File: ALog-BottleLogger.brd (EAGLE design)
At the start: 120.7 x 44.5 mm, 106 parts, among them IC2 ATMEGA644M, J6 5.5x2.1mm Barrel, Q10 MOSFET_PCH-IRLML2244, Q11 MOSFET-NCH-BSS138, Q12 MOSFET_PCH-IRLML2244, Q5 MOSFET_PCH-IRLML2244, Q7 MOSFET_PCH-IRLML2244, Q8 MOSFET-NCH-BSS138, Q9 MOSFET-NCH-BSS138, U2 FT231X-Q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

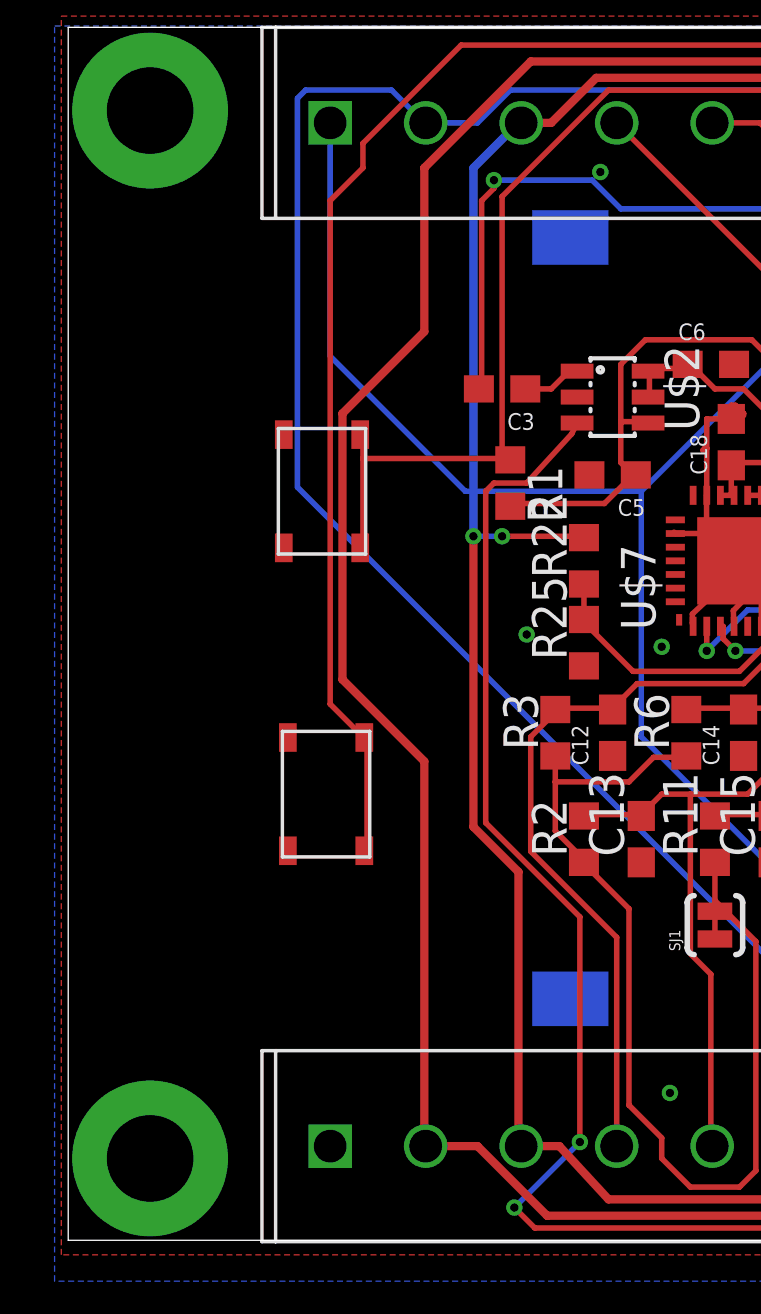
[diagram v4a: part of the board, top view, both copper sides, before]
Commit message: update botton pad sizes
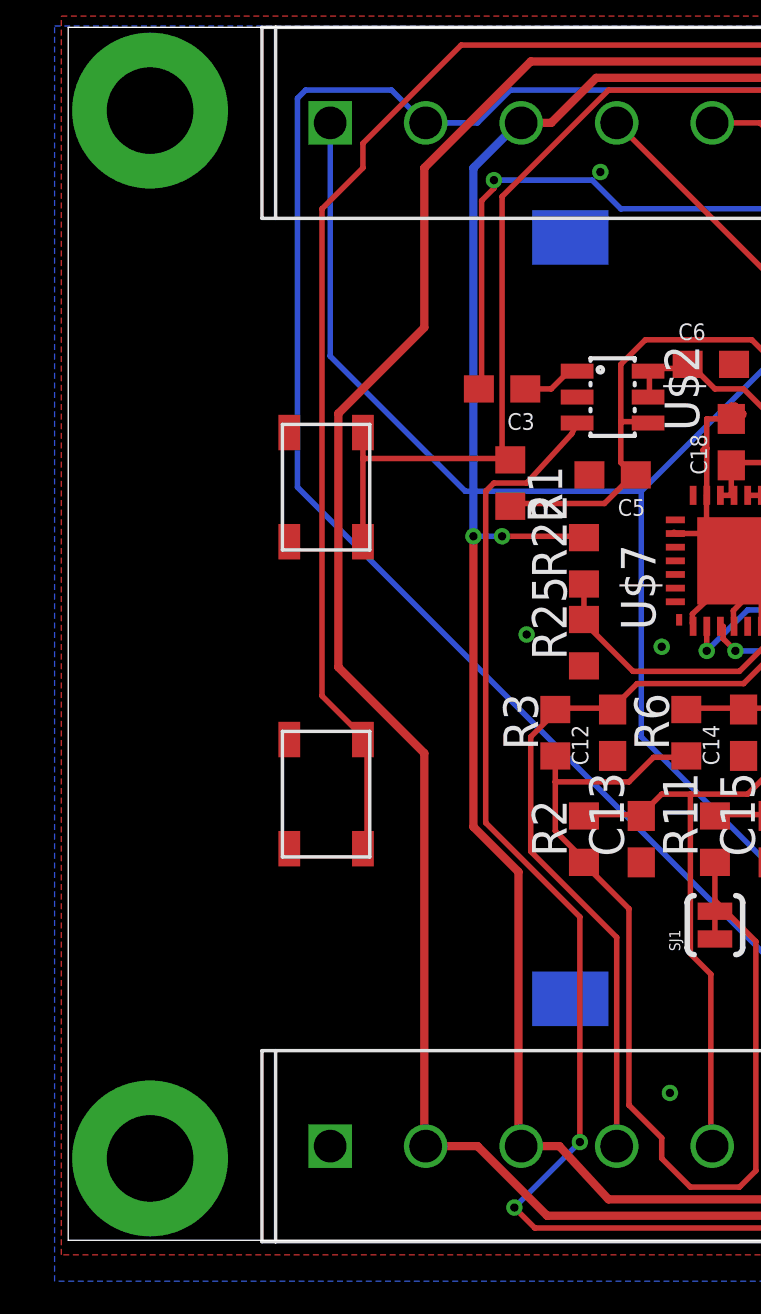
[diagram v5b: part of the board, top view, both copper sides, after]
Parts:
- S1, U$4: value SKRPABE010 -> SWITCHC&K_400GF; device bschulz:SKRPABE010_(SWITCH) -> bschulz_Old:SWITCH_4.2X3.2
- moved U$4 0.21 mm to (9.45, 27.6)
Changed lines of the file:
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@@
 <?xml version="1.0" encoding="utf-8"?>
 <!DOCTYPE eagle SYSTEM "eagle.dtd">
-<eagle version="8.4.3">
+<eagle version="8.4.1">
 <drawing>
 <settings>
@@
 <attribute name="VALUE_PART" value="10k" x="16.2" y="27.75" size="1.778" layer="27" rot="R270" display="off"/>
 </element>
-<element name="U$4" library="bschulz" package="SKRPABE010_(SWITCH)" value="SKRPABE010" x="9.3" y="27.45" rot="R90"/>
+<element name="U$4" library="bschulz_Old" package="SWITCH_4.2X3.2" value="SWITCHC&amp;K_400GF" x="9.45" y="27.6" rot="R90">
+<attribute name="DIGIKEY" value="CKN10504CT-ND" x="9.45" y="27.6" size="1.778" layer="27" rot="R90" display="off"/>
+<attribute name="MF" value="C&amp;K" x="9.45" y="27.6" size="1.778" layer="27" rot="R90" display="off"/>
+<attribute name="MPN" value="PTS810 SJG 250 SMTR LFS" x="9.45" y="27.6" size="1.778" layer="27" rot="R90" display="off"/>
+</element>
 <element name="Q5" library="bschulz" package="SOT23-3" value="MOSFET_PCH-IRLML2244" x="63.15" y="30.3" smashed="yes" rot="R90">
 <attribute name="DIGIKEY" value="FDN360PCT-ND" x="63.15" y="30.3" size="1.778" layer="27" rot="R90" display="off"/>
@@
 <attribute name="VALUE" x="88.175" y="18.255" size="0.6096" layer="27" rot="R270"/>
 </element>
-<element name="S1" library="bschulz" package="SKRPABE010_(SWITCH)" value="SKRPABE010" x="9.45" y="16.35" rot="R270"/>
+<element name="S1" library="bschulz_Old" package="SWITCH_4.2X3.2" value="SWITCHC&amp;K_400GF" x="9.45" y="16.35" rot="R270">
+<attribute name="DIGIKEY" value="CKN10504CT-ND" x="9.45" y="16.35" size="1.778" layer="27" rot="R270" display="off"/>
+<attribute name="MF" value="C&amp;K" x="9.45" y="16.35" size="1.778" layer="27" rot="R270" display="off"/>
+<attribute name="MPN" value="PTS810 SJG 250 SMTR LFS" x="9.45" y="16.35" size="1.778" layer="27" rot="R270" display="off"/>
+</element>
 <element name="R18" library="bschulz_passives" package="R0603" value="1.62M" x="88.65" y="23.1">
 <attribute name="DIGIKEY" value="541-1.62MHCT-ND" x="88.65" y="23.1" size="1.778" layer="27" display="off"/>
@@
 <contactref element="U$4" pad="P$4"/>
 <contactref element="IC2" pad="4"/>
-<wire x1="10.8" y1="29.4" x2="10.8" y2="28.65" width="0.2032" layer="1"/>
-<wire x1="10.8" y1="28.65" x2="10.8" y2="25.5" width="0.2032" layer="1"/>
-<wire x1="10.8" y1="25.5" x2="10.7" y2="25.375" width="0.2032" layer="1"/>
-<wire x1="10.8" y1="29.4" x2="10.7" y2="29.525" width="0.2032" layer="1"/>
+<wire x1="10.8" y1="29.6" x2="10.8" y2="28.65" width="0.2032" layer="1"/>
+<wire x1="10.8" y1="28.65" x2="10.8" y2="25.6" width="0.2032" layer="1"/>
+<wire x1="10.8" y1="25.5" x2="10.8" y2="25.6" width="0.2032" layer="1"/>
 <wire x1="10.8" y1="28.65" x2="15.9" y2="28.65" width="0.2032" layer="1"/>
 <wire x1="15.9" y1="28.65" x2="16.2" y2="28.65" width="0.2032" layer="1"/>
@@
 <wire x1="68.4" y1="0.75" x2="98.1" y2="0.75" width="0.3048" layer="1"/>
 <wire x1="65.7" y1="3.45" x2="68.4" y2="0.75" width="0.3048" layer="1"/>
-<wire x1="13.05" y1="39.3" x2="13.05" y2="33.3" width="0.3048" layer="1"/>
-<wire x1="10.05" y1="30.3" x2="13.05" y2="33.3" width="0.3048" layer="1"/>
-<wire x1="10.05" y1="20.55" x2="10.05" y2="30.3" width="0.3048" layer="1"/>
-<wire x1="13.05" y1="17.55" x2="10.05" y2="20.55" width="0.3048" layer="1"/>
-<wire x1="13.05" y1="3.45" x2="13.05" y2="17.55" width="0.3048" layer="1"/>
+<wire x1="13.05" y1="39.3" x2="13.05" y2="33.45" width="0.3048" layer="1"/>
+<wire x1="9.9" y1="30.3" x2="13.05" y2="33.45" width="0.3048" layer="1"/>
+<wire x1="9.9" y1="21" x2="9.9" y2="30.3" width="0.3048" layer="1"/>
+<wire x1="13.05" y1="17.85" x2="9.9" y2="21" width="0.3048" layer="1"/>
+<wire x1="13.05" y1="3.45" x2="13.05" y2="17.85" width="0.3048" layer="1"/>
 <wire x1="13.05" y1="3.45" x2="13.1" y2="3.45" width="0.2032" layer="1"/>
 <via x="98.1" y="0.75" extent="1-16" drill="0.3048" shape="octagon"/>
@@
 <contactref element="D1" pad="3"/>
 <wire x1="10.95" y1="18.3" x2="10.95" y2="14.4" width="0.2032" layer="1"/>
-<wire x1="10.95" y1="14.4" x2="10.85" y2="14.275" width="0.2032" layer="1"/>
-<wire x1="10.95" y1="18.3" x2="10.85" y2="18.425" width="0.2032" layer="1"/>
+<wire x1="10.95" y1="14.4" x2="10.8" y2="14.35" width="0.2032" layer="1"/>
+<wire x1="10.95" y1="18.3" x2="10.8" y2="18.35" width="0.2032" layer="1"/>
 <wire x1="92.25" y1="19.65" x2="92.25" y2="16.8" width="0.2032" layer="1"/>
 <wire x1="94.2" y1="21.6" x2="92.25" y2="19.65" width="0.2032" layer="1"/>
@@
 <wire x1="10.8" y1="40.2" x2="14.4" y2="43.8" width="0.2032" layer="1"/>
 <wire x1="10.8" y1="39.3" x2="10.8" y2="40.2" width="0.2032" layer="1"/>
-<wire x1="9.6" y1="38.1" x2="10.8" y2="39.3" width="0.2032" layer="1"/>
-<wire x1="9.6" y1="19.65" x2="9.6" y2="38.1" width="0.2032" layer="1"/>
-<wire x1="10.8" y1="18.45" x2="9.6" y2="19.65" width="0.2032" layer="1"/>
+<wire x1="9.3" y1="37.8" x2="10.8" y2="39.3" width="0.2032" layer="1"/>
+<wire x1="9.3" y1="19.95" x2="9.3" y2="37.8" width="0.2032" layer="1"/>
+<wire x1="10.8" y1="18.45" x2="9.3" y2="19.95" width="0.2032" layer="1"/>
 <wire x1="92.25" y1="16.8" x2="92.15" y2="16.8" width="0.2032" layer="1"/>
-<wire x1="10.8" y1="18.45" x2="10.85" y2="18.425" width="0.2032" layer="1"/>
+<wire x1="10.8" y1="18.45" x2="10.8" y2="18.35" width="0.2032" layer="1"/>
 <via x="97.8" y="27.6" extent="1-16" drill="0.3048"/>
 <via x="99.9" y="29.7" extent="1-16" drill="0.3048"/>

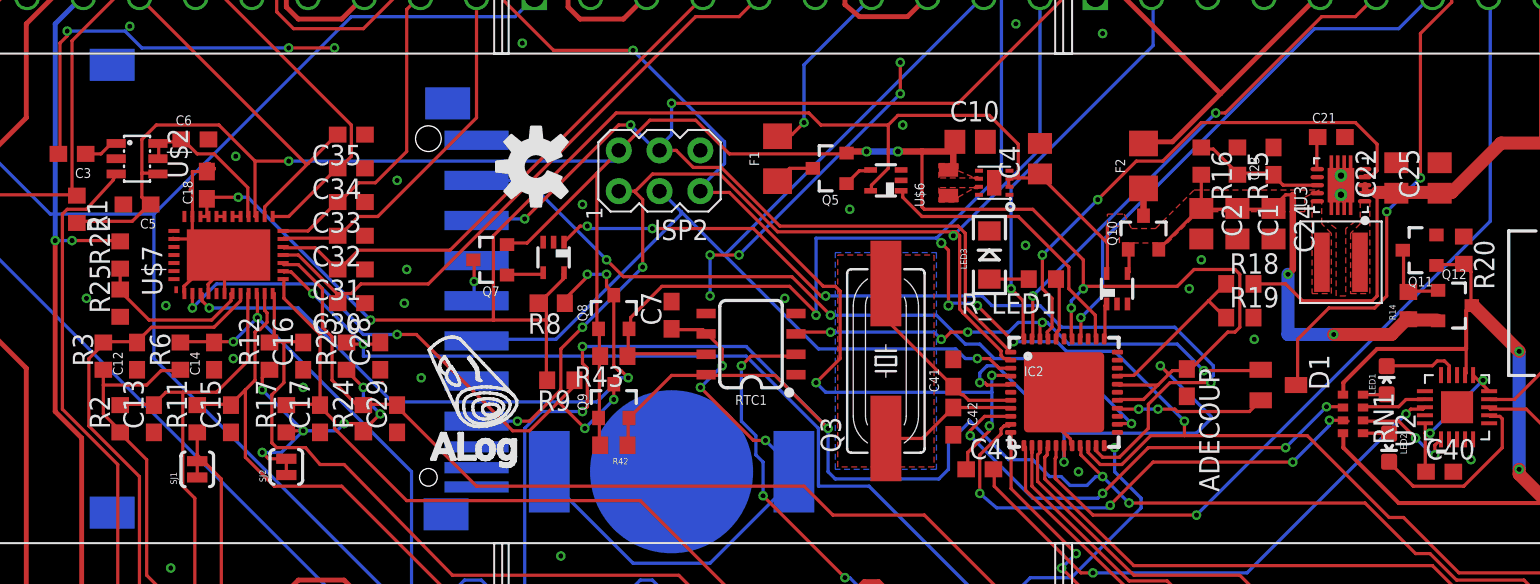
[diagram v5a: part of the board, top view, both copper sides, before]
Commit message: Cleanup and PDF creation
Cleaned up and updated old parts, added frames to schematic, printed schematic to PDF
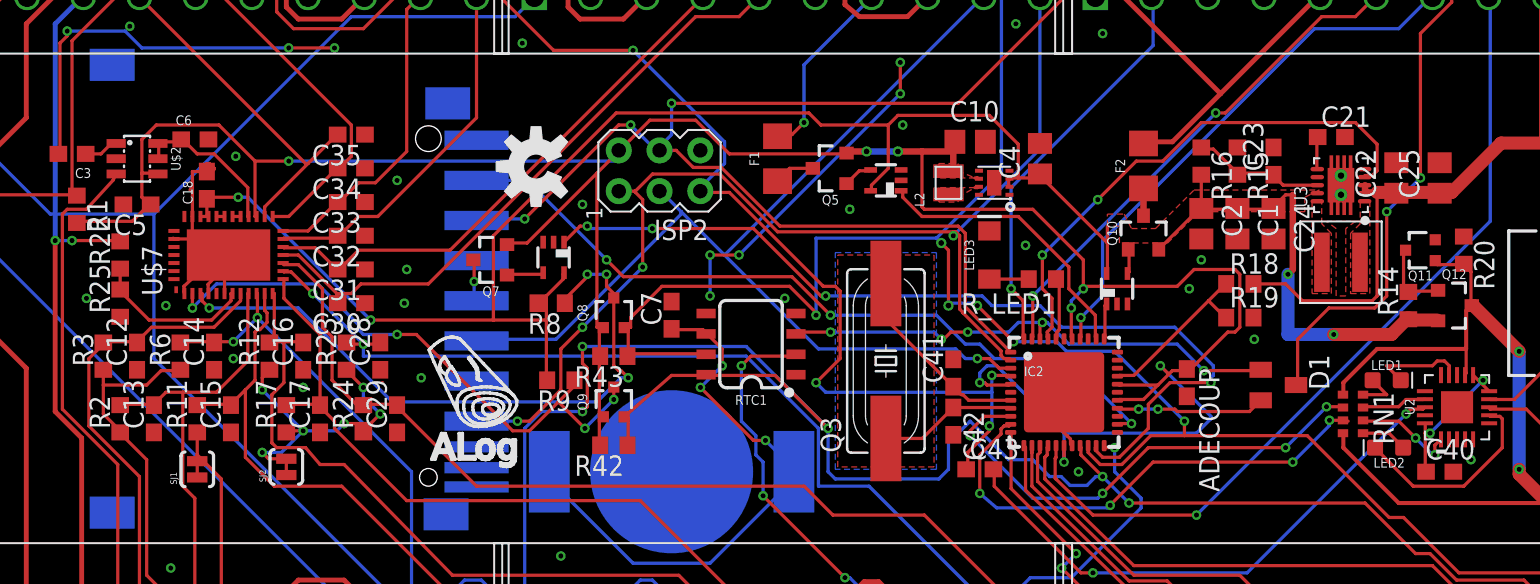
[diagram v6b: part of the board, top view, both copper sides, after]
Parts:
- removed U$6: 74404020022, csandell:WURTH2.2UF
- added L2: 2.2uH, bschulz:0806
- D+, D-: value 27ohm -> 27
- Q10, Q12, Q5, Q7: value MOSFET_PCH-IRLML2244 -> FDN360P
- Q11, Q8: value MOSFET-NCH-BSS138 -> 310mA/60V/1.6Ω; device bschulz:SOT23-3 -> bschulz:SOT323
- Q9: value MOSFET-NCH-BSS138 -> 2N7002; device bschulz:SOT23-3 -> bschulz:SOT323
- renumbered U$9 to L1
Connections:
- net +3V3: now also L2.P$2; no longer U$6.2
- net N$1: now also L2.P$1; no longer U$6.1
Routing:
- net N$33: track 11.4 -> 12.6 mm
- net N$35: track 4.75 -> 5.99 mm
- net N$3: track 1.50 -> 2.73 mm
- net N$2: track 1.65 -> 2.88 mm
- net +3V3: track 171.0 -> 171.8 mm
